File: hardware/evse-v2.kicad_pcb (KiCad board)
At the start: 4 copper layers, 74 x 115 mm, 133 parts, among them J101 Boot, P101 CON-SENSOR2, P102 Relay, P103 L'+PE, P104 L'+PE, P105 CP/PP/PE, P106 Power, P107 Motor, P108 Switch_LED, P109 Enable, P110 MODBUS, P111 DC-Protect, P112 DC-Protect, P113 GP, Q101 2N7002P, Q102 SI2305CDS-T1-GE3, Q103 2N7002P, Q104 2N7002P, SW101 OS103011MS8QP1, SW102 OS103011MS8QP1, U101 XMC1404, U102 PEM1-S12-D12-S, U105 OPA171AIDBV, U106 A5950GLP, U108 AQH3213AX, U109 HCPL2731, U110 TPS70933DBVR, U111 IRM02-12, U112 WPMDL110, U113 SP3491, X101 16MHz

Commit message: add hint
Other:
- board text added: "DC has 5V PWM!"

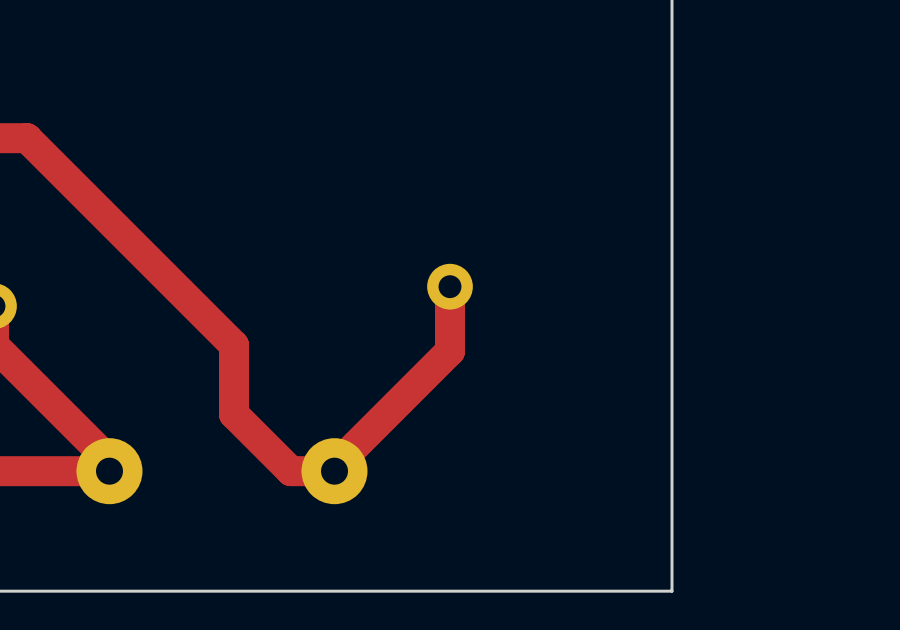
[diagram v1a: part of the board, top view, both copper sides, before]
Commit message: fix footprint
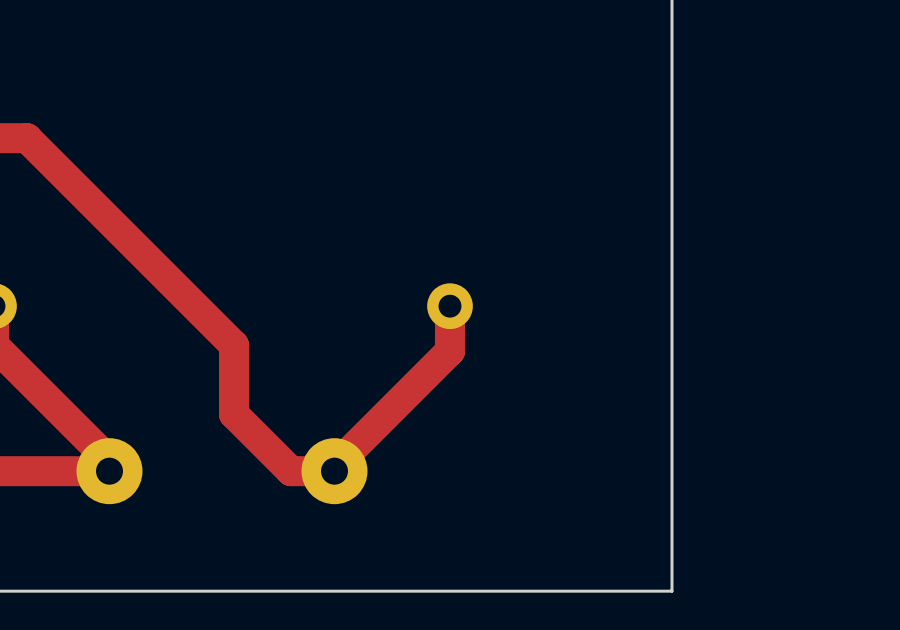
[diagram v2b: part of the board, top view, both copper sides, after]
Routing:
- net L: track 84.1 -> 83.4 mm

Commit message: add todos
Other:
- board text added: "5V Ideal Diode?"
- board text added: "Fixme"

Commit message: add hint
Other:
- board text added: "Add P0.2. Debug"

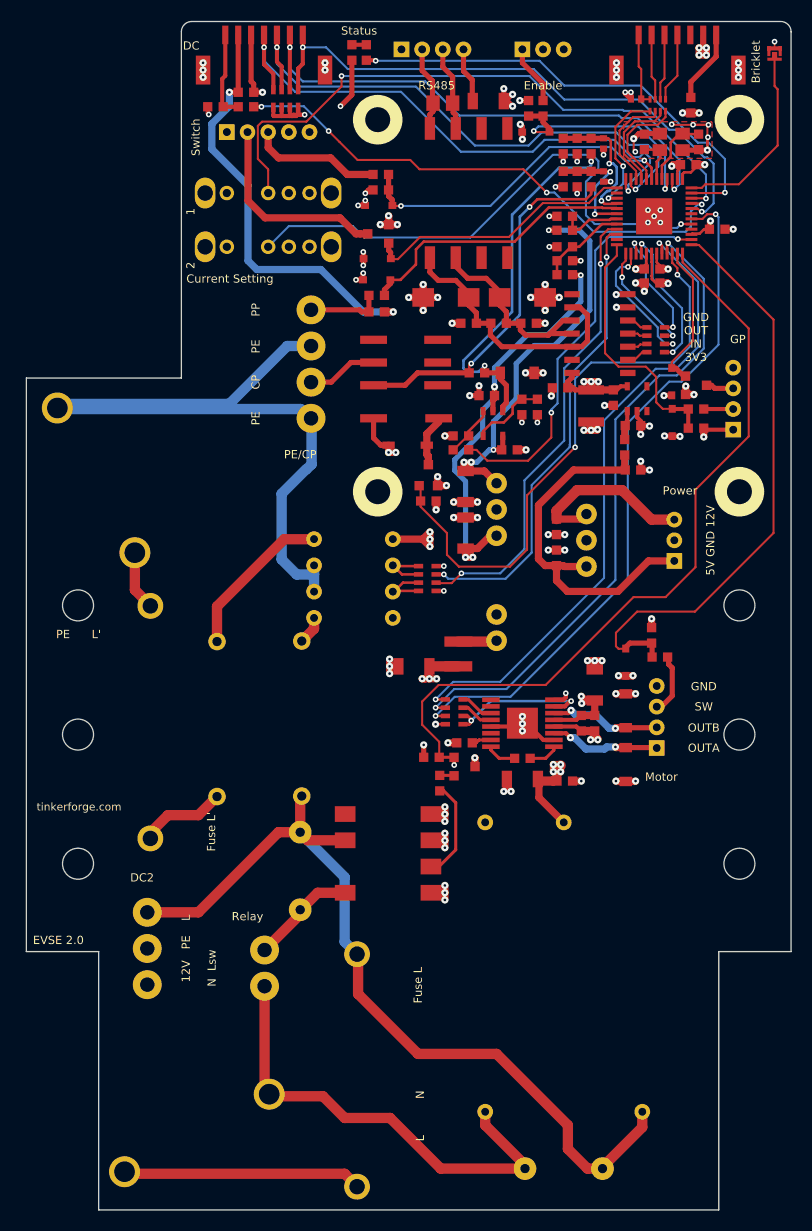
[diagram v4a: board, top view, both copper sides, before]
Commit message: start working at version 2.1
changes:
 * remove dc protector connector for alc
 * move relay connector
 * Move PE/CP connector
 * move Fuse L, PE L' connector, R
 * add Logos
 * change PCB outline to give more space
 * move pcb edge connectors (enable etc.)
 * remove DC Protection PWM signal
 * add 220uH
 * fix relay footprint bug
 * move din rail mounting
 * move PCB drills
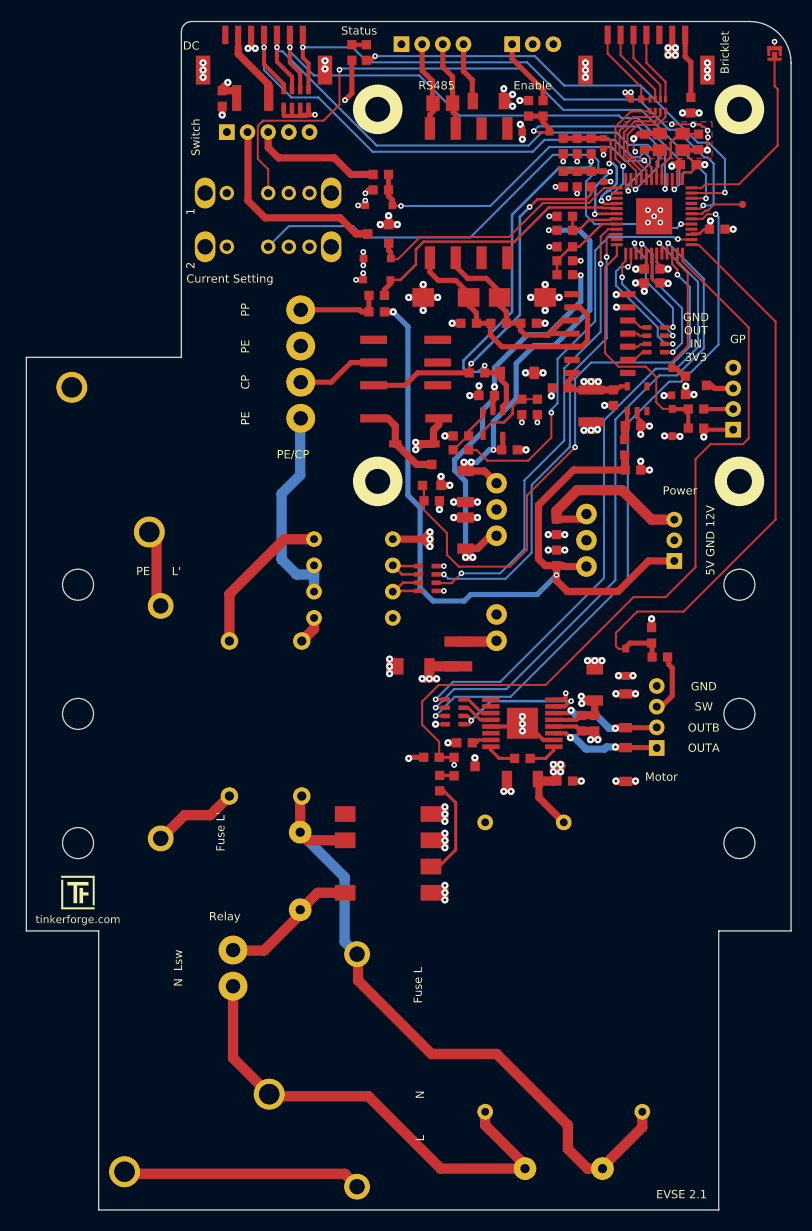
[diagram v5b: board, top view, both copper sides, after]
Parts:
- removed R133: 1k, kicad-libraries:R0603F
- removed R140: 100, kicad-libraries:R0603F
- added G***: LOGO, kicad-libraries:Logo_31x31, F.Cu at (82.3, 135.8)
- added L105: 744032221, kicad-libraries:1210, F.Cu at (99.2, 59.0)
- C107: value 100nF -> 1uF; footprint C0603F -> kicad-libraries:C0603F
- D107: value ‎PESD5V0L1BA -> ‎PESD3V3L1BA
- P111: value DC-Protect -> Debug; footprint kicad-libraries:OQ_3P_Vertical -> kicad-libraries:DEBUG_PAD
- moved P111 92.2 mm to (146.7, 69.2), turned to 0 degrees
- moved P102 3.05 mm to (97.3, 143.2)
- moved P101 3.00 mm to (137.3, 57.6)
- moved P104 2.44 mm to (89.2, 101.0)
- moved C107 2.38 mm to (96.3, 59.0), turned to 270 degrees
- moved A105 2.00 mm to (146.3, 118.5)
- moved A106 2.00 mm to (82.3, 118.5)
- moved R118 1.20 mm to (97.0, 119.0)
- moved P109 1.12 mm to (126.3, 53.8)
- moved A101 1.00 mm to (146.3, 96.0)
- moved A102 1.00 mm to (111.3, 96.0)
- moved A103 1.00 mm to (111.3, 60.0)
- moved A104 1.00 mm to (146.3, 60.0)
- moved F102 1.00 mm to (90.3, 119.3)
- moved P105 1.00 mm to (103.9, 84.7)
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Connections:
- C107 pad 1: GND -> 5V
- C107 pad 2: 5V -> GND
- P111 pad 1: VCC -> Net-(P111-Pad1)
- P112 pad 6: 5V -> Net-(L105-Pad1)
- REL101 pad 2: CPOUT -> Net-(REL101-Pad2)
- REL101 pad 3: CPOUT2 -> Net-(REL101-Pad3)
- REL101 pad 6: Net-(REL101-Pad6) -> CPOUT2
- REL101 pad 7: Net-(REL101-Pad7) -> CPOUT
- U101 pad 31: Net-(U101-Pad31) -> Net-(P111-Pad1)
- U101 pad 33: DC-PWM -> Net-(U101-Pad33)
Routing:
- net GND: track 266.4 -> 171.1 mm, vias 128 -> 130
- net VCC: track 279.1 -> 226.2 mm
- net DC-PWM: track 51.4 -> 0.00 mm, vias 4 -> 0
- net L: track 83.4 -> 64.7 mm
- net Net-(P112-Pad7): track 8.57 -> 0.00 mm
- net Net-(L105-Pad1): track 0.00 -> 7.32 mm
- net 5V: track 193.1 -> 186.2 mm, vias 4 -> 5
- net Net-(P111-Pad1): track 0.00 -> 5.31 mm
- net Net-(D112-Pad1): track 5.07 -> 8.57 mm
- net Net-(P102-Pad2): track 10.4 -> 13.4 mm
- net Net-(F102-Pad1): track 5.62 -> 7.66 mm
- net P0_5: track 60.5 -> 62.5 mm
- net RELAY: track 75.2 -> 77.1 mm
- net 3V3: track 105.7 -> 104.1 mm, vias 28 -> 27
- net Net-(P101-Pad6): track 6.52 -> 7.74 mm
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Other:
- outline, holes or cut-outs redrawn
- board text added: "EVSE 2.1"
- board text removed: "12V PE L"
- board text removed: "Add P0.2. Debug"
- board text removed: "DC has 5V PWM!"
- board text removed: "DC2"
- board text removed: "EVSE 2.0"
- board text removed: "Fixme"

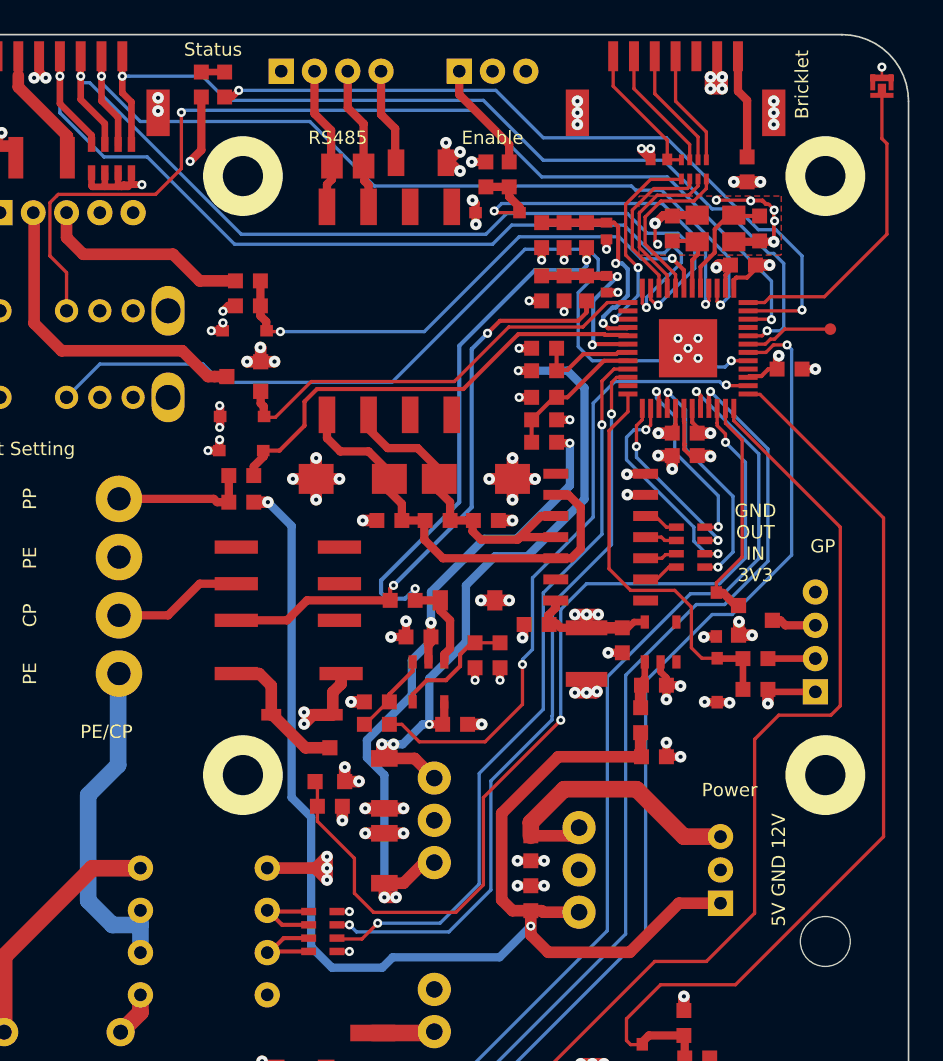
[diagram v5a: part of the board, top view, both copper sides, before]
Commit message: add ideal diode
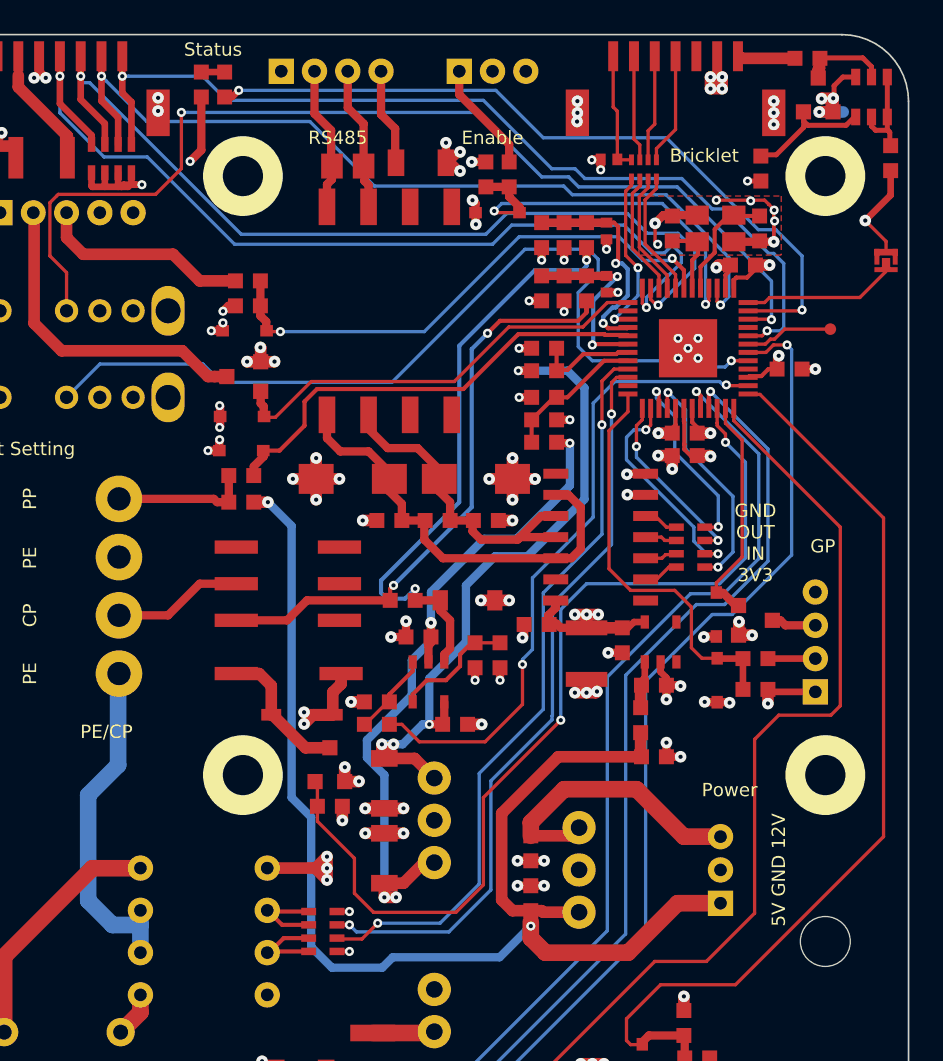
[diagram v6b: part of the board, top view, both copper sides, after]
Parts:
- added Q105: SSM3J355R,LF, kicad-libraries:SOT23GDS, F.Cu at (145.9, 55.2)
- added R133: 47k, kicad-libraries:R0603F, F.Cu at (142.5, 59.6)
- added R140: 10k, kicad-libraries:R0603F, F.Cu at (150.3, 59.0)
- added U103: DMMT5401, kicad-libraries:SOT26, F.Cu at (149.1, 55.3)
- moved J101 10.5 mm to (150.0, 65.1)
- moved L103 7.60 mm to (145.3, 53.0), turned to 180 degrees
- moved C101 3.00 mm to (133.3, 59.0)
- moved RP101 3.00 mm to (135.4, 59.6)
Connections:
- L103 pad 1: 5V -> Net-(L103-Pad1)
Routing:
- net 5V: track 186.2 -> 271.7 mm, vias 5 -> 6
- net BOOT: track 18.9 -> 9.56 mm
- net Net-(Q105-PadG): track 0.00 -> 7.67 mm
- net Net-(R140-Pad2): track 0.00 -> 5.92 mm
- net Net-(L103-Pad1): track 0.00 -> 5.18 mm
- net GND: track 171.1 -> 175.7 mm, vias 130 -> 131
- net Net-(L103-Pad2): track 6.23 -> 3.40 mm
- net S-MOSI: track 9.85 -> 7.42 mm
- net S-CS: track 10.0 -> 7.63 mm
- net S-CLK: track 9.76 -> 7.40 mm
- net S-MISO: track 12.6 -> 10.3 mm
- net Net-(C101-Pad1): track 8.41 -> 7.16 mm
- net Net-(P101-Pad6): track 7.74 -> 6.49 mm
- net Net-(P101-Pad5): track 7.28 -> 6.39 mm
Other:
- board text added: "74mm = 4TE"
- board text removed: "54mm = 3TE"
- board text removed: "5V Ideal Diode?"

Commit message: detail improvements
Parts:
- moved C107 4.25 mm to (100.5, 59.0)
- moved L105 1.58 mm to (97.7, 59.0), turned to 0 degrees
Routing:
- net 5V: track 271.7 -> 265.6 mm
- net VCC: track 226.2 -> 223.1 mm
- net DC-X30: track 55.8 -> 55.2 mm

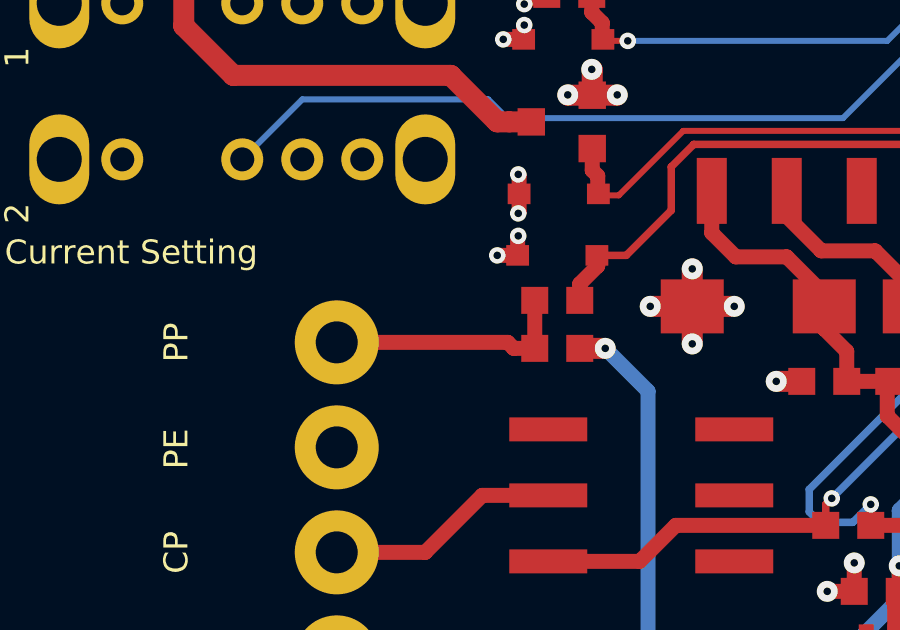
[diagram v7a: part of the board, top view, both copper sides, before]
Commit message: add pulldown for pp
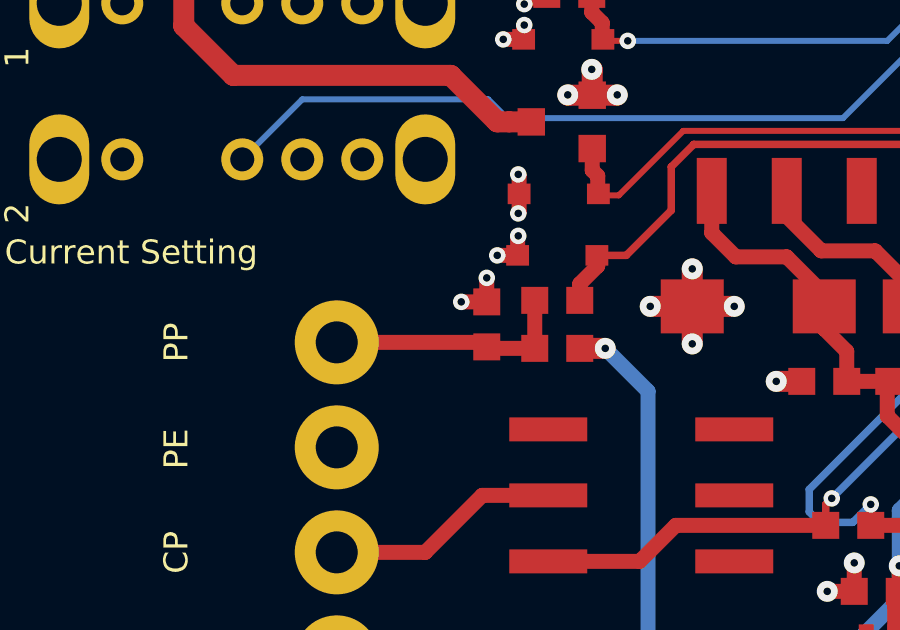
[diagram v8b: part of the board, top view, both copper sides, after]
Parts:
- added R141: 2k, kicad-libraries:R0603F, F.Cu at (108.9, 78.8)
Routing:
- net GND: track 175.8 -> 177.5 mm, vias 131 -> 133
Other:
- board text added: "TBD Pulldown"
